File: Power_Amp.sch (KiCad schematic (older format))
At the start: 56 parts, among them J10 TEST_1P, J11 TEST_1P, J12 TEST_1P, J13 TEST_1P, J14 TEST_1P, J15 TEST_1P, J16 TEST_1P, J9 TEST_1P, U4 AD8620, U5 AD8620

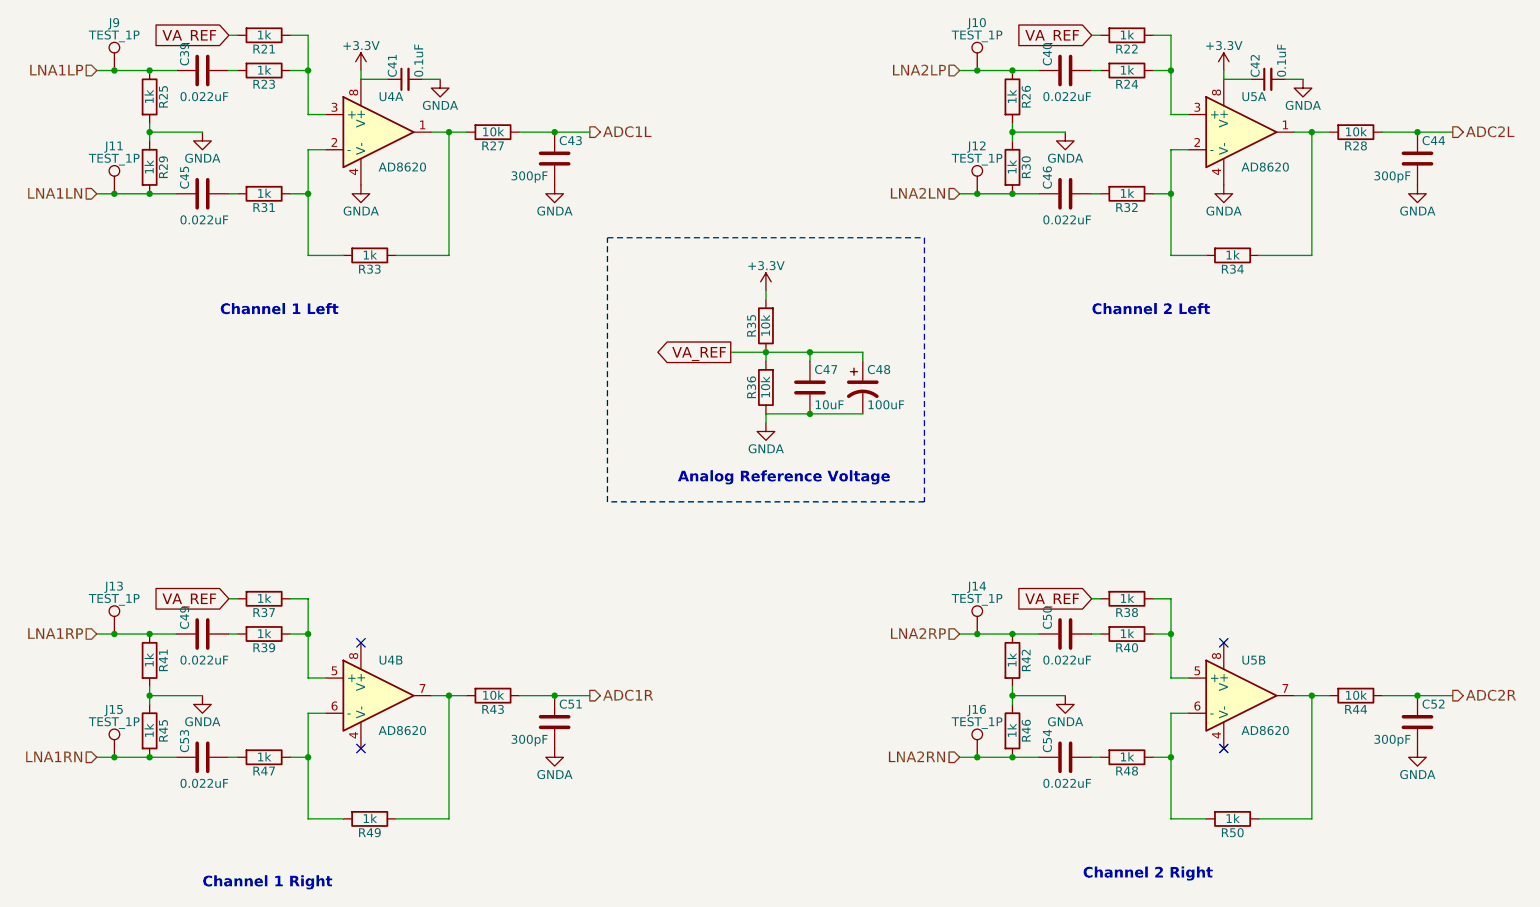
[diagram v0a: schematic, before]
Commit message: Change OPAMP number to OPA2365
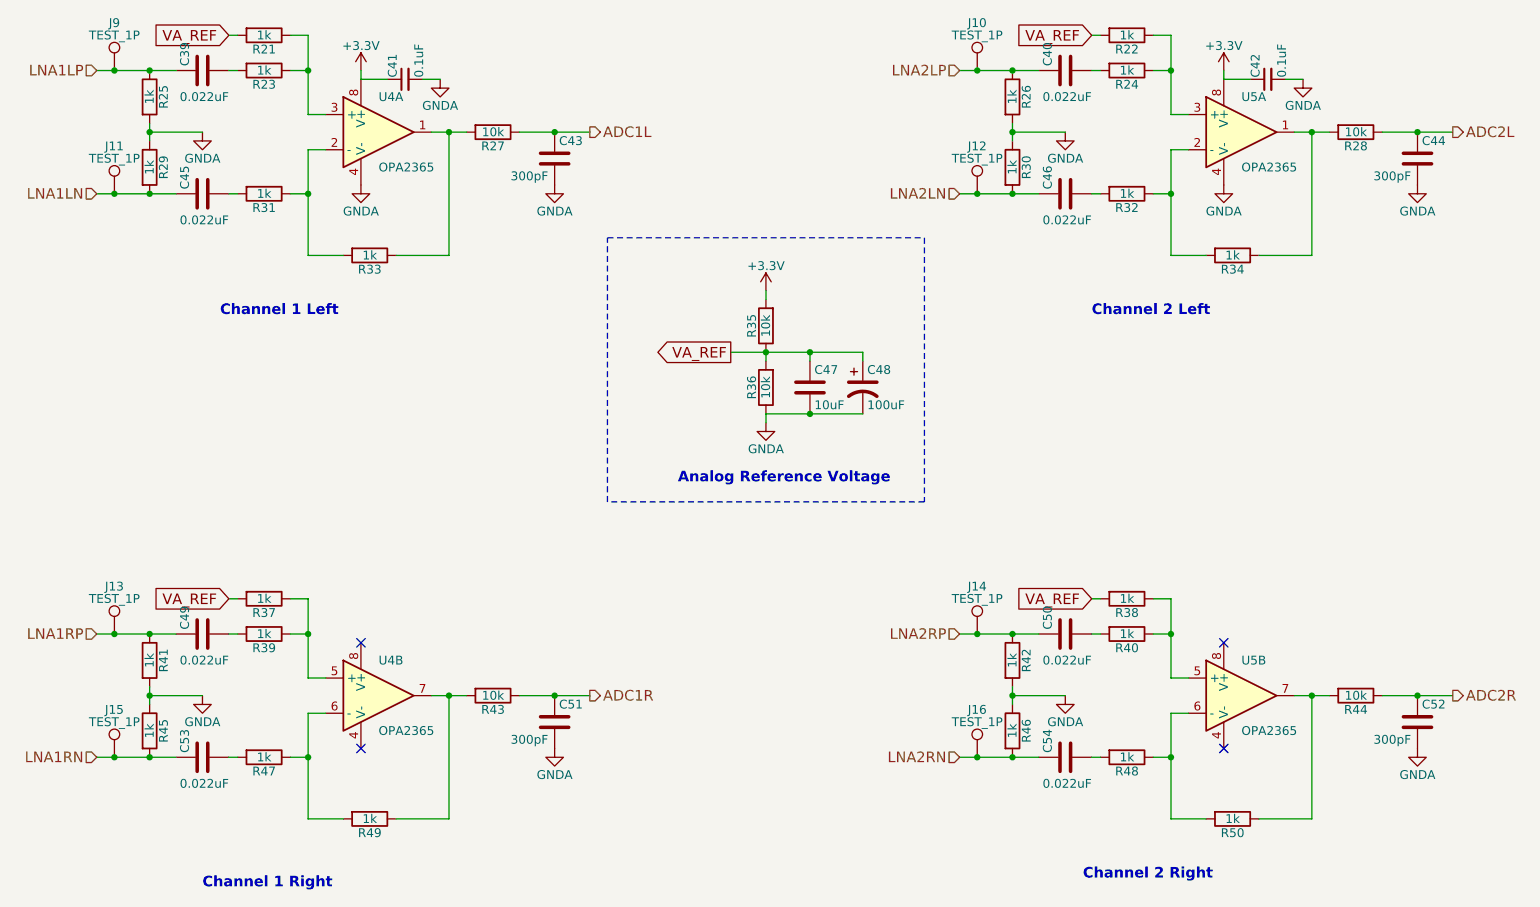
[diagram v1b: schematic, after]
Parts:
- U4, U5: value AD8620 -> OPA2365
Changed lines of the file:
@@
 P 3600 1900
 F 0 "U4" H 3600 2100 50  0000 L CNN
-F 1 "AD8620" H 3600 1700 50  0000 L CNN
+F 1 "OPA2365" H 3600 1700 50  0000 L CNN
 F 2 "" H 3600 1900 50  0001 C CNN
 F 3 "" H 3600 1900 50  0001 C CNN
@@
 P 3600 5100
 F 0 "U4" H 3600 5300 50  0000 L CNN
-F 1 "AD8620" H 3600 4900 50  0000 L CNN
+F 1 "OPA2365" H 3600 4900 50  0000 L CNN
 F 2 "" H 3600 5100 50  0001 C CNN
 F 3 "" H 3600 5100 50  0001 C CNN
@@
 P 8500 1900
 F 0 "U5" H 8500 2100 50  0000 L CNN
-F 1 "AD8620" H 8500 1700 50  0000 L CNN
+F 1 "OPA2365" H 8500 1700 50  0000 L CNN
 F 2 "" H 8500 1900 50  0001 C CNN
 F 3 "" H 8500 1900 50  0001 C CNN
@@
 P 8500 5100
 F 0 "U5" H 8500 5300 50  0000 L CNN
-F 1 "AD8620" H 8500 4900 50  0000 L CNN
+F 1 "OPA2365" H 8500 4900 50  0000 L CNN
 F 2 "" H 8500 5100 50  0001 C CNN
 F 3 "" H 8500 5100 50  0001 C CNN

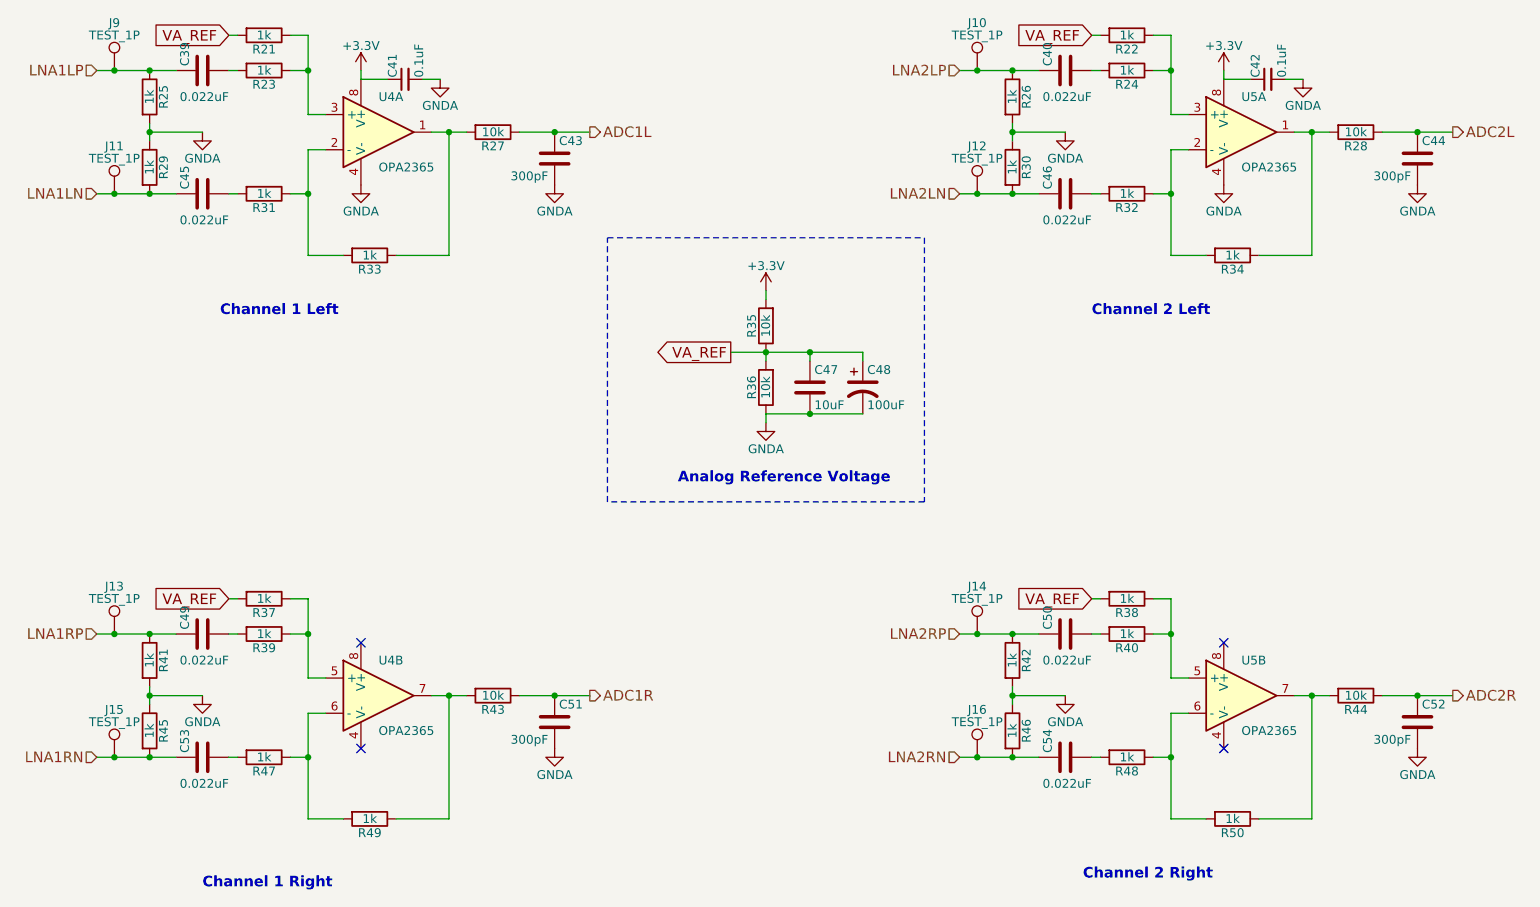
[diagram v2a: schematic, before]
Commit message: Assigned footprint for dimension checking
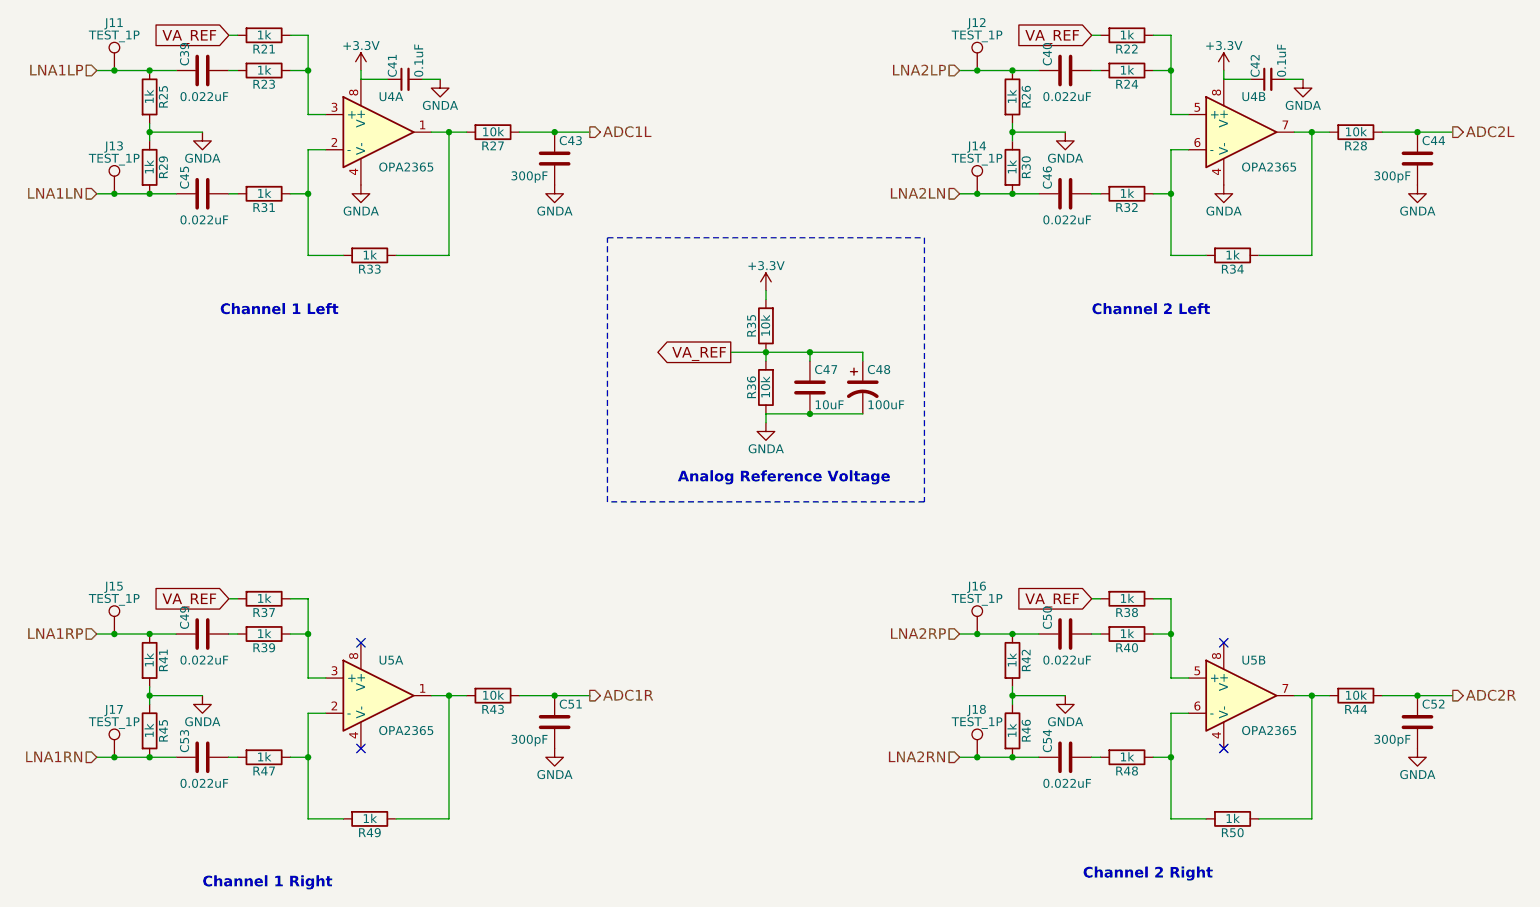
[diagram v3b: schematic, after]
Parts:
- C39, C40, C41, C42, C43, C44, C45, C46, C49, C50, C51, C52, C53, C54: footprint (none) -> Capacitors_SMD:C_0603_HandSoldering
- C47: footprint (none) -> Capacitors_SMD:C_0805_HandSoldering
- C48: footprint (none) -> Capacitors_SMD:C_1206_HandSoldering
- J11: renamed from J9; footprint (none) -> Pin_Headers:Pin_Header_Straight_1x01_Pitch2.54mm
- J12: renamed from J10; footprint (none) -> Pin_Headers:Pin_Header_Straight_1x01_Pitch2.54mm
- J13: renamed from J11; footprint (none) -> Pin_Headers:Pin_Header_Straight_1x01_Pitch2.54mm
- J14: renamed from J12; footprint (none) -> Pin_Headers:Pin_Header_Straight_1x01_Pitch2.54mm
- J15: renamed from J13; footprint (none) -> Pin_Headers:Pin_Header_Straight_1x01_Pitch2.54mm
- J16: renamed from J14; footprint (none) -> Pin_Headers:Pin_Header_Straight_1x01_Pitch2.54mm
- J17: renamed from J15; footprint (none) -> Pin_Headers:Pin_Header_Straight_1x01_Pitch2.54mm
- J18: renamed from J16; footprint (none) -> Pin_Headers:Pin_Header_Straight_1x01_Pitch2.54mm
- R21, R22, R23, R24, R25, R26, R27, R28, R29, R30, R31, R32, R33, R34, R35, R36, R37, R38, R39, R40, R41, R42, R43, R44, R45, R46, R47, R48, R49, R50: footprint (none) -> Resistors_SMD:R_0603_HandSoldering
- U4, U5: footprint (none) -> Housings_SOIC:SOIC-8_3.9x4.9mm_Pitch1.27mm
- U4: renamed from U5; footprint (none) -> Housings_SOIC:SOIC-8_3.9x4.9mm_Pitch1.27mm
- U5: renamed from U4; footprint (none) -> Housings_SOIC:SOIC-8_3.9x4.9mm_Pitch1.27mm
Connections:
- net at R37.1, R39.1: now also U5.3 (+); no longer U5.5 (+)
- net at R47.1, R49.2: now also U5.2 (-); no longer U5.6 (-)
- net at R43.2, R49.1: now also U5.1; no longer U5.7
- net at R28.2, R34.1: now also U4.7; no longer U4.1
- net at R32.1, R34.2: now also U4.6 (-); no longer U4.2 (-)
- net at R22.1, R24.1: now also U4.5 (+); no longer U4.3 (+)

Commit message: First released
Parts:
- C48: footprint Capacitors_SMD:C_1206_HandSoldering -> Capacitors_SMD:C_1210_HandSoldering
- renumbered U5 to U4, U4 to U5
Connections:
- net at R43.2, R49.1: now also U4.7; no longer U4.1
- net at R47.1, R49.2: now also U4.6 (-); no longer U4.2 (-)
- net at R37.1, R39.1: now also U4.5 (+); no longer U4.3 (+)
- net at R22.1, R24.1: now also U5.3 (+); no longer U5.5 (+)
- net at R32.1, R34.2: now also U5.2 (-); no longer U5.6 (-)
- net at R28.2, R34.1: now also U5.1; no longer U5.7
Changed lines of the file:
@@
 Connection ~ 4600 1900
 $Comp
-L AD8620 U5
-U 1 1 5AD8B056
+L AD8620 U4
+U 2 1 5AD8B056
 P 3600 5100
-F 0 "U5" H 3600 5300 50  0000 L CNN
+F 0 "U4" H 3600 5300 50  0000 L CNN
 F 1 "OPA2365" H 3600 4900 50  0000 L CNN
 F 2 "Housings_SOIC:SOIC-8_3.9x4.9mm_Pitch1.27mm" H 3600 5100 50  0001 C CNN
 F 3 "" H 3600 5100 50  0001 C CNN
-	1    3600 5100
+	2    3600 5100
 	1    0    0    -1
 $EndComp
@@
 Connection ~ 4600 5100
 $Comp
-L AD8620 U4
-U 2 1 5AD8BACD
+L AD8620 U5
+U 1 1 5AD8BACD
 P 8500 1900
-F 0 "U4" H 8500 2100 50  0000 L CNN
+F 0 "U5" H 8500 2100 50  0000 L CNN
 F 1 "OPA2365" H 8500 1700 50  0000 L CNN
 F 2 "Housings_SOIC:SOIC-8_3.9x4.9mm_Pitch1.27mm" H 8500 1900 50  0001 C CNN
 F 3 "" H 8500 1900 50  0001 C CNN
-	2    8500 1900
+	1    8500 1900
 	1    0    0    -1
 $EndComp
@@
 F 0 "C48" H 6375 3450 50  0000 L CNN
 F 1 "100uF" H 6375 3250 50  0000 L CNN
-F 2 "Capacitors_SMD:C_1206_HandSoldering" H 6350 3350 50  0001 C CNN
+F 2 "Capacitors_SMD:C_1210_HandSoldering" H 6350 3350 50  0001 C CNN
 F 3 "" H 6350 3350 50  0001 C CNN
 	1    6350 3350
